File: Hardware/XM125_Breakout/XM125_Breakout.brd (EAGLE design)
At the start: 25.4 x 50.8 mm, 105 parts, among them J13 SWD (DNP), J2 RIGHT_ANGLE, J3 RIGHT_ANGLE, U1 XM125, U2 RT9080-33GJ5, U3 RT9080-18GJ5, U4 CH340C, U5 ESD Diode

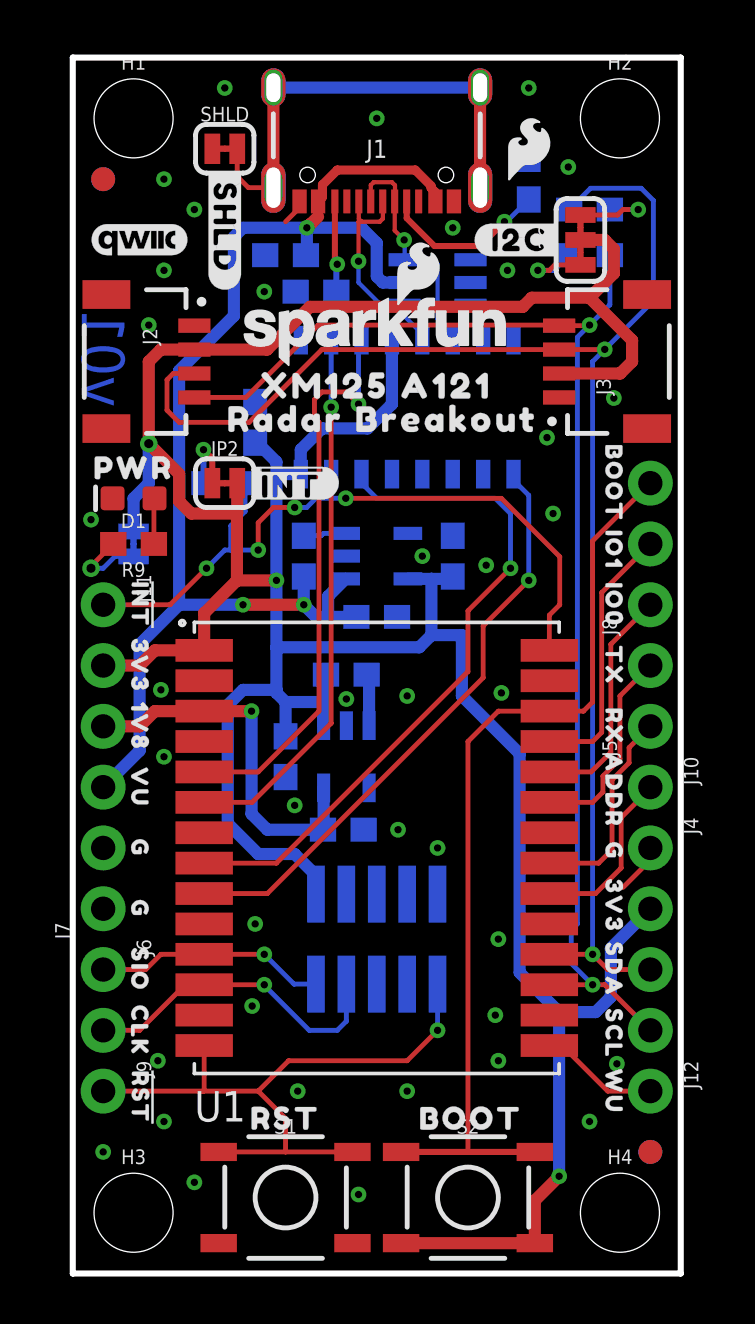
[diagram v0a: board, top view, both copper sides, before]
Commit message: Initial commit for v10 red boards; adjusted firmware files
Small changes made for board - removed EN pullups, changed button part number; no need for distance and presence file differentiation - just run with binaries in the original SDK; added STM32CubeIDEProject files for testing
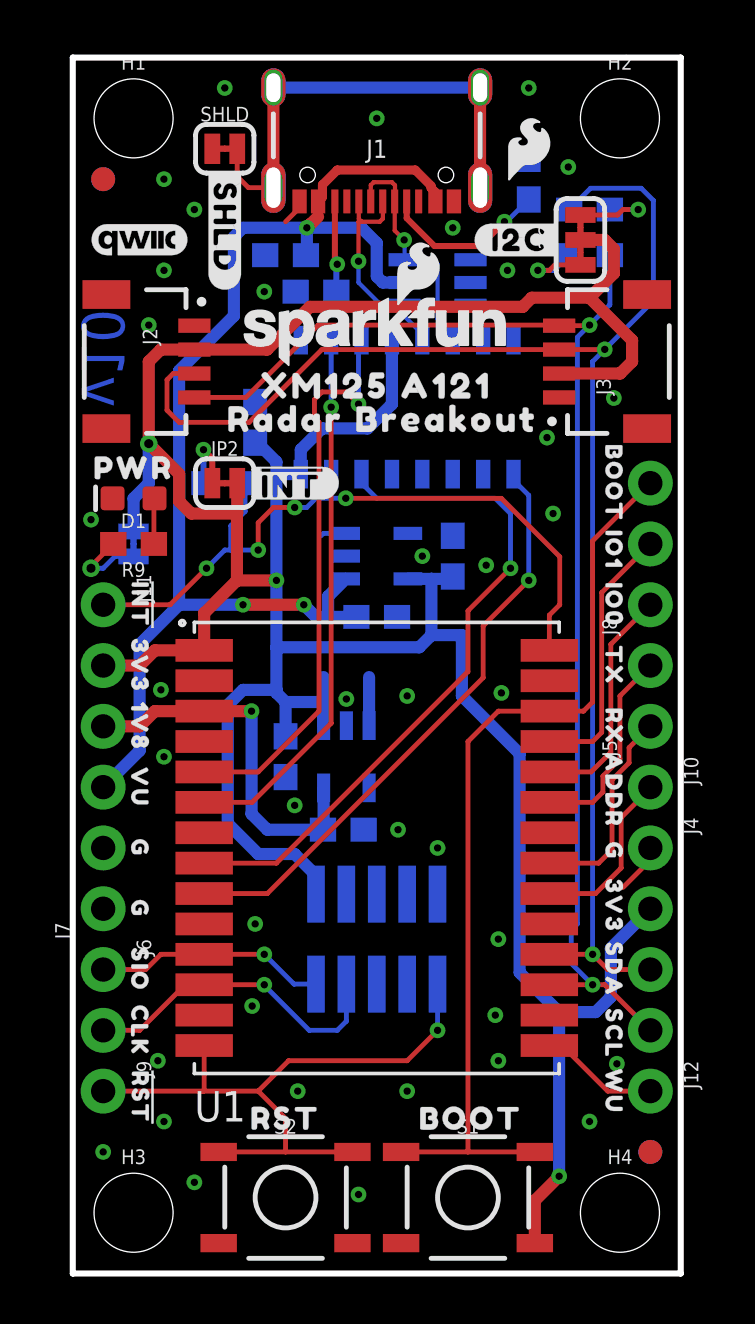
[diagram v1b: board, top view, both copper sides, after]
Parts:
- removed R1, R4: 100k, SparkFun-Resistors:0603
- moved S1 7.62 mm to (16.5, 3.17)
- moved S2 7.62 mm to (8.89, 3.17)
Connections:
- removed net N$13: R1.2, U2.3
- removed net N$20: R4.2, U3.3
- net !XM125_RESET: now also S2.1, S2.2; no longer S1.1, S1.2
- net 3.3V: now also S1.3, S1.4, U3.3; no longer R4.1, S2.3, S2.4
- net GND: now also S2.3, S2.4; no longer S1.3, S1.4
- net V_USB: now also U2.3; no longer R1.1
- net XM125_GPIO2/BOOT0: now also S1.1, S1.2; no longer S2.1, S2.2
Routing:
- net 3.3V: track 147.4 -> 143.7 mm
- net N$20: track 2.17 -> 0.00 mm
- net N$13: track 1.79 -> 0.00 mm
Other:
- board text added: "v10"
- board text removed: "v01"

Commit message: Changes for reds review completed; panel files added
Changes for review have been made; panelized files have been added
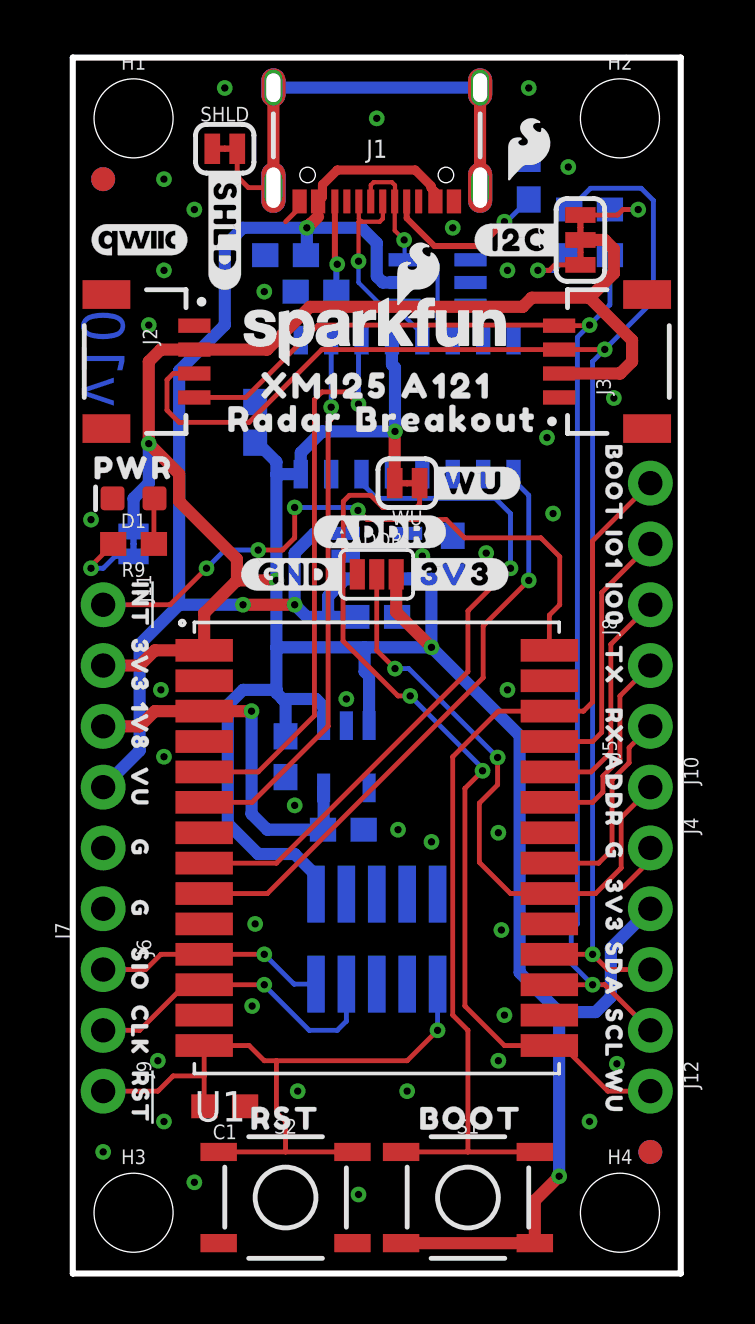
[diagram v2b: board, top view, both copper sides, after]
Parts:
- removed JP2: JUMPER-SMT_2_NC_TRACE_SILK, SparkFun-Jumpers:SMT-JUMPER_2_NC_TRACE_SILK
- removed R13: 10k, SparkFun-Resistors:0603
- added ADDR: JUMPER-SMT_3_NO_SILK, SparkFun-Jumpers:SMT-JUMPER_3_NO_SILK
- added C1: 0.1uF, SparkFun-Capacitors:0603
- added U$22: (no value), output:#WU#14
- added U$50: (no value), output:#GND#17
- added U$9: (no value), output:#3V3#17
- added WU: JUMPER-SMT_2_NC_TRACE_SILK, SparkFun-Jumpers:SMT-JUMPER_2_NC_TRACE_SILK
- U$25: device output:##INT#8 -> output:#ADDR#16
- moved U$25 4.21 mm to (12.8, 31.0)
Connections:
- removed net N$18: JP2.1, R13.2
- net !XM125_INT: no longer R13.1
- net !XM125_RESET: now also C1.2
- net 3.3V: now also ADDR.3, WU.2; no longer JP2.2
- net GND: now also ADDR.1, C1.1
- net WAKE_UP: now also WU.1
- net XM125_I2C_ADDRESS: now also ADDR.2
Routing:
- net WAKE_UP: track 5.01 -> 37.8 mm, vias 0 -> 2
- net XM125_I2C_ADDRESS: track 7.33 -> 25.6 mm, vias 0 -> 2
- net 3.3V: track 143.7 -> 152.9 mm, vias 3 -> 5
- net V_USB: track 53.9 -> 57.5 mm
- net !XM125_INT: track 29.7 -> 26.4 mm
- net N$18: track 2.96 -> 0.00 mm, vias 1 -> 0
- net !XM125_RESET: track 27.5 -> 29.1 mm
- net XM125_GPIO2/BOOT0: track 38.8 -> 39.3 mm
- net GND: vias 38 -> 39
